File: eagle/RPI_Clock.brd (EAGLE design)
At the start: 157.5 x 54.3 mm, 27 parts, among them T1 IN-12, T2 IN-12, T3 IN-12, T4 IN-12, T5 IN-12, T6 IN-12, U1 K155ID1, U11 74HC595, U2 K155ID1, U3 K155ID1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

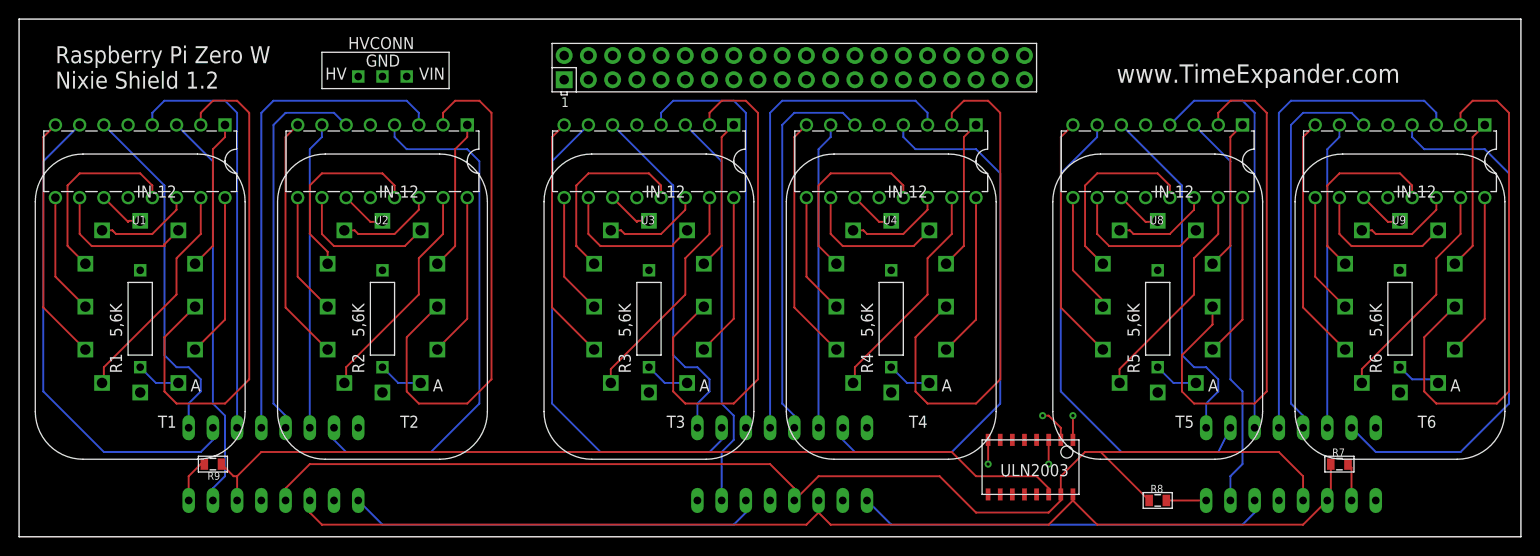
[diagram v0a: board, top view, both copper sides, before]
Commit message: Updated Eagle design files with 1.3 version
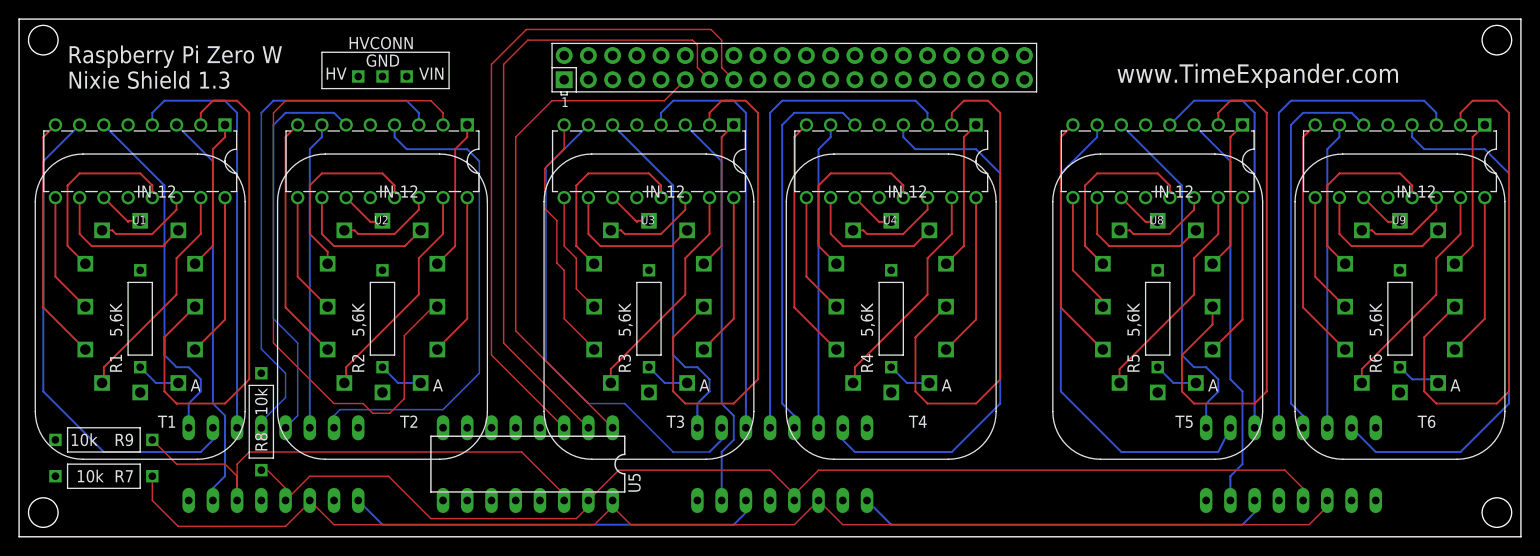
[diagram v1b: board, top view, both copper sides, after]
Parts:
- removed ULN2003: ULN2003D1013TR, EE_copy:SO16-NARROW
- added U5: ULN2003A, TimeExpander:DIL16
- R7, R8, R9: device EE_copy:0805 -> TimeExpander:ANODE_RESISTOR
- moved R7 124.5 mm to (14.0, 6.35), turned to 180 degrees
- moved R8 94.0 mm to (25.4, 6.99), turned to 90 degrees
- moved R9 6.84 mm to (14.0, 10.2)
- renumbered U$1 to U10
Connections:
- net +5V: now also R7.P$2, R8.P$2, R9.P$2; no longer R7.2, R8.2, R9.2
- net GND: now also U5.8; no longer ULN2003.8
- net N$47: now also U5.1; no longer ULN2003.1
- net N$48: now also U5.2; no longer ULN2003.2
- net N$49: now also R7.P$1, U5.16; no longer R7.1, ULN2003.16
- net N$50: now also R8.P$1, U5.15; no longer R8.1, ULN2003.15
- net N$51: now also R9.P$1, U5.14; no longer R9.1, ULN2003.14
- net N$52: now also U5.3; no longer ULN2003.3
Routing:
- net N$51: track 93.1 -> 54.1 mm
- net N$47: track 83.7 -> 55.0 mm, vias 1 -> 0
- net N$12: track 56.0 -> 73.0 mm
- net N$49: track 119.8 -> 134.9 mm
- net +5V: track 13.7 -> 0.00 mm
- net N$50: track 128.8 -> 121.4 mm
- net N$74: track 55.8 -> 51.8 mm
- net GND: track 2.54 -> 0.00 mm, vias 1 -> 0
- net N$48: track 70.0 -> 67.5 mm, vias 1 -> 0
- net N$71: track 51.9 -> 54.0 mm
- net N$77: track 52.5 -> 50.8 mm
- net N$72: track 40.9 -> 42.0 mm
- net N$30: track 25.9 -> 26.5 mm
- net N$11: track 5.22 -> 4.68 mm
- net N$52: track 72.3 -> 72.0 mm, vias 1 -> 0
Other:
- board text added: "Raspberry Pi Zero W Nixie Shield 1.3"
- board text removed: "Raspberry Pi Zero W Nixie Shield 1.2"
